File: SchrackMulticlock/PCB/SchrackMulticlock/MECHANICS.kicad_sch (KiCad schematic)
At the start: 22 parts, among them J2 MEM2067-02-180-00-A_REVB, SW2 SW_Push, SW3 SW_Push, SW4 SW_Push, SW5 SW_Push, SW6 SW_Push

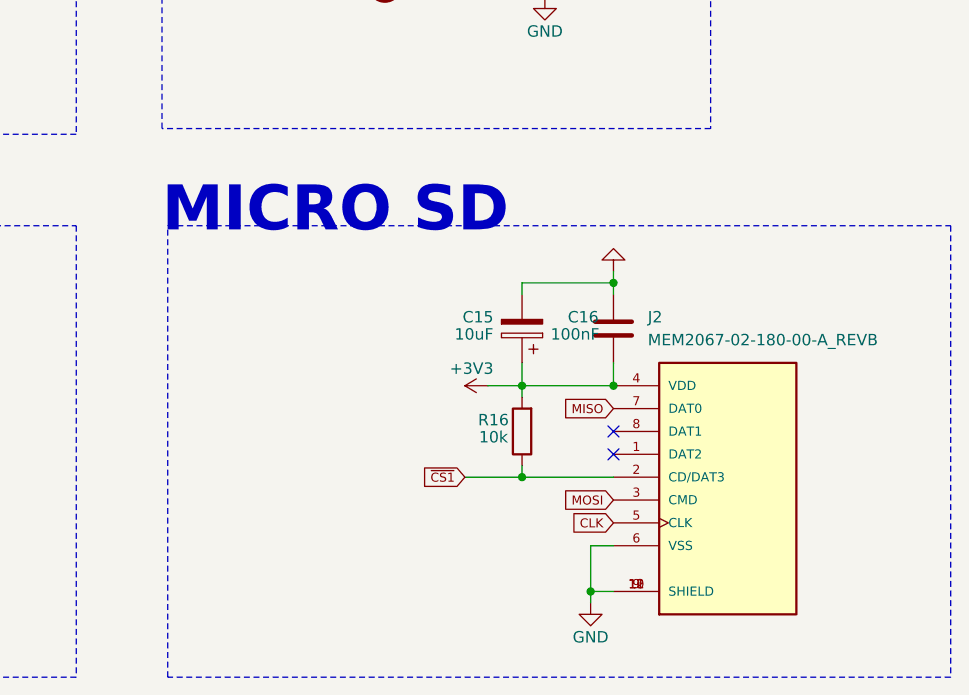
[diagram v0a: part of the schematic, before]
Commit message: SchrackMulticlock and Counter update
Schematic update for both
PCB update for Counter
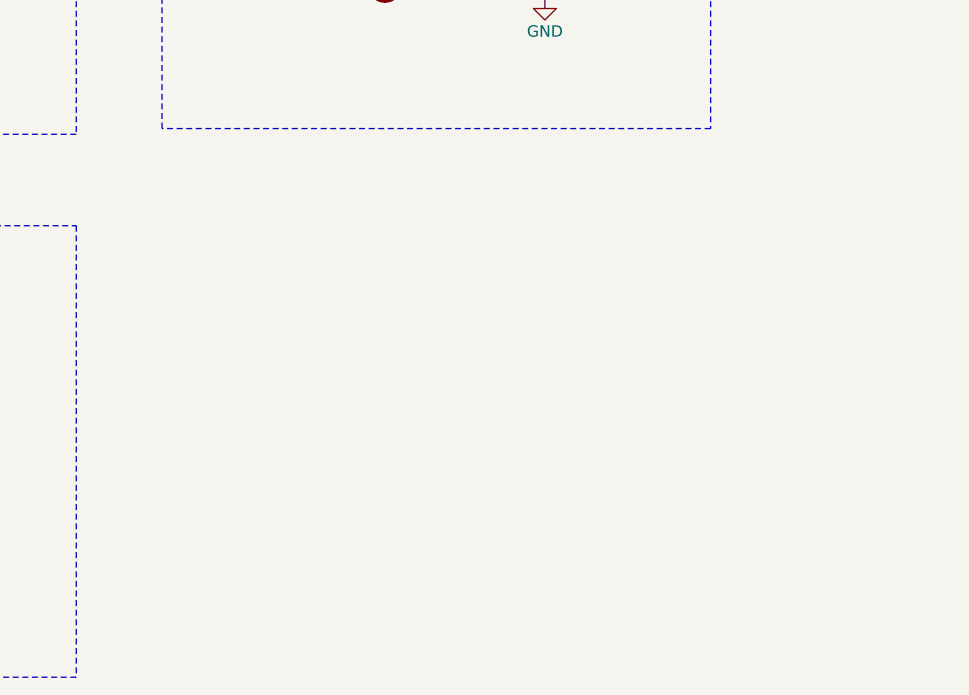
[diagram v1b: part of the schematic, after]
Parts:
- removed C15: 10uF, Capacitor_Tantalum_SMD:CP_EIA-3216-18_Kemet-A_Pad1.58x1.35mm_HandSolder, symbol Device:C_Polarized
- removed C16: 100nF, Capacitor_SMD:C_0805_2012Metric_Pad1.18x1.45mm_HandSolder, symbol Device:C
- removed J2: MEM2067-02-180-00-A_REVB, Schrack_brd:MICRO_SD_CARD, symbol SchrackThingy_library:MEM2067-02-180-00-A_REVB
- removed R16: 10k, Resistor_SMD:R_0805_2012Metric_Pad1.20x1.40mm_HandSolder, symbol Device:R
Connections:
- no-connect marks 2 -> 0
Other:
- note removed: "MICRO SD"

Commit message: schrack multiclock schematic update
Just regular updates
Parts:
- removed C10, C11, C13: 100nF, Capacitor_SMD:C_0805_2012Metric_Pad1.18x1.45mm_HandSolder, symbol Device:C
- removed R12, R13, R15: 2k, Resistor_SMD:R_0805_2012Metric_Pad1.20x1.40mm_HandSolder, symbol Device:R
- removed SW2, SW3, SW4: SW_Push, Connector_JST:JST_XH_B2B-XH-A_1x02_P2.50mm_Vertical, symbol Switch:SW_Push
- added C? (x3): 100nF, Capacitor_SMD:C_0805_2012Metric_Pad1.18x1.45mm_HandSolder, symbol Device:C
- added R? (x6): 10k, Resistor_SMD:R_0805_2012Metric_Pad1.20x1.40mm_HandSolder, symbol Device:R
- added SW? (x3): SW_Push, Connector_JST:JST_XH_B2B-XH-A_1x02_P2.50mm_Vertical, symbol Switch:SW_Push
- added U? (x7): 74HC14, Package_SO:SOIC-14_3.9x8.7mm_P1.27mm, symbol 74xx:74HC14
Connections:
- net +3V3: now also R?.2, R?.2, R?.2, U?.14 (VCC)
- net GND: now also C?.1, C?.1, C?.1, SW?.1, SW?.1, SW?.1, U?.7 (GND)
- net MODE: now also U?.6
- net RESET: now also U?.4
- new net: C?.2, R?.1, U?.3
- new net: C?.2, R?.1, U?.5
- new net: C?.2, R?.1, U?.1
- new net AUX: U?.2
- new net MD: R?.1, R?.2, SW?.2
- new net RST: R?.1, R?.2, SW?.2
- new net SCH_SW: R?.1, R?.2, SW?.2
- no-connect marks 0 -> 6
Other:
- note removed: "DEBOUNCE: 100nF and 2k?"

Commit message: SchrackMulticlock schematic
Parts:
- added C12, C15, C16: 100nF, Capacitor_SMD:C_0805_2012Metric_Pad1.18x1.45mm_HandSolder, symbol Device:C
- added R14, R17, R20, R21, R23, R24: 10k, Resistor_SMD:R_0805_2012Metric_Pad1.20x1.40mm_HandSolder, symbol Device:R
- added SW4, SW6, SW7: SW_Push, Connector_JST:JST_XH_B2B-XH-A_1x02_P2.50mm_Vertical, symbol Switch:SW_Push
- gave numbers to parts that had none: 13
- renumbered C12 to C13, C14 to C17, R14 to R18, SW5 to SW8, SW6 to SW9
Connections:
- net SCH_SW is gone; now on net MD: R19.1, R22.2, SW5.2
- net +3V3: now also R14.2, R20.2, R21.2
- net AUX: now also U8.10; no longer U8.2
- net GND: now also C12.1, C15.1, C16.1, SW4.1, SW6.1, SW7.1
- net MD: no longer R12.1, R15.2, SW2.2
- net MODE: now also U8.2; no longer U8.6
- net DIGIT_SELECT: now reaches U8.8
- net at U8.9: now also C12.2, R17.1
- net at U8.11: now also C15.2, R23.1
- net TIME_DOWN: now reaches U8.12
- net at U8.13: now also C16.2, R24.1
- net RESET renamed BTN2
- net RST renamed BT2
- net BT2: now also R14.1, R17.2, R20.1, R21.1, R23.2, R24.2, SW4.2, SW6.2, SW7.2
- new net BT1: R12.1, R15.2, SW2.2
- new net BTN1: U8.6
- no-connect marks 6 -> 0
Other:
- note added: "BTN1 press - digit++ BTN1 hold - digit select BTN2 press - start/stop (by context) BTN2 hold - reset MODE - ctu/ctd switch"
- note added: "harder for me to make it work in program..."
- note added: "the PCB is going to be much smaller, less reason to use the Schrack Box If the box is not going to be big, there is no reason to use SchrackButtons"
- note removed: "PREDIFINED TIME, CHANGING USING WEBSERVER"
- moved on the sheet: U8D, U8E, U8F, U8G

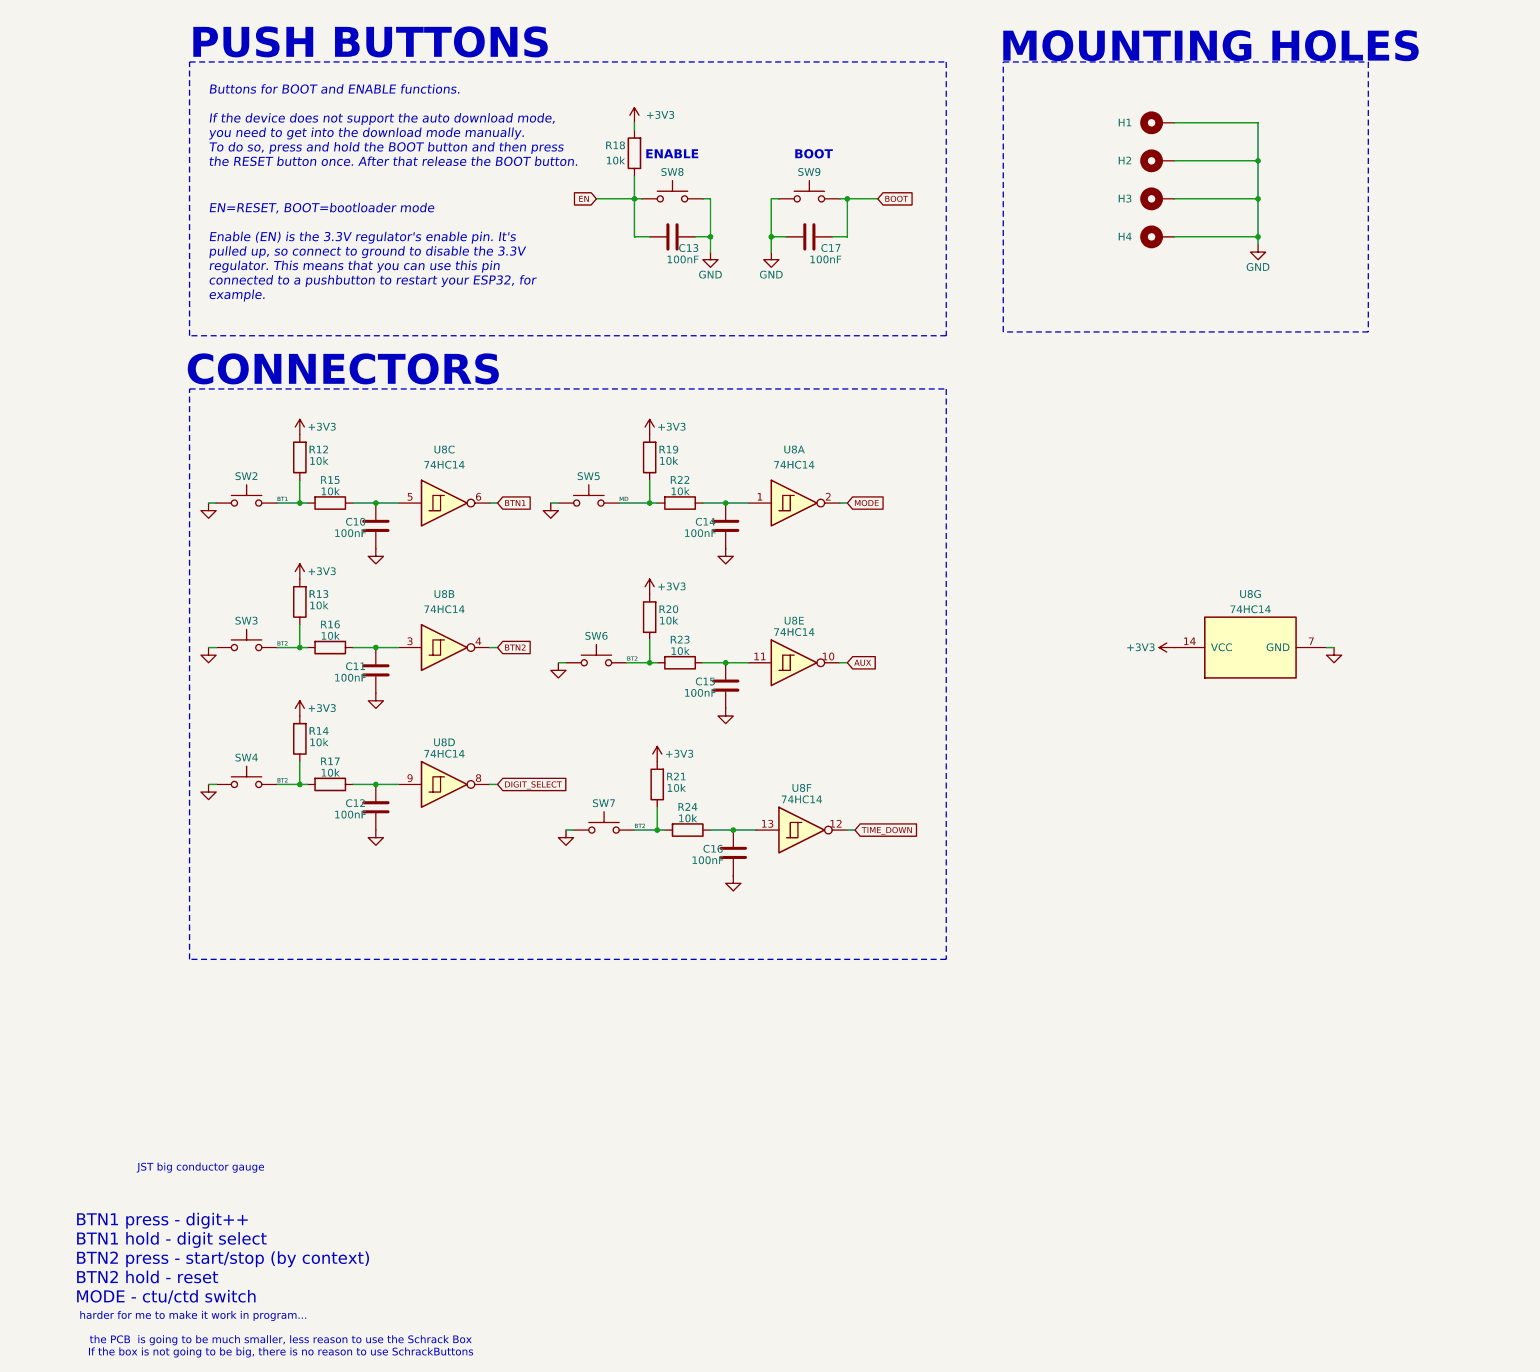
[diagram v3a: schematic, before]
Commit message: Schrackcounter Prototype update
Schematic + PCB update, final version
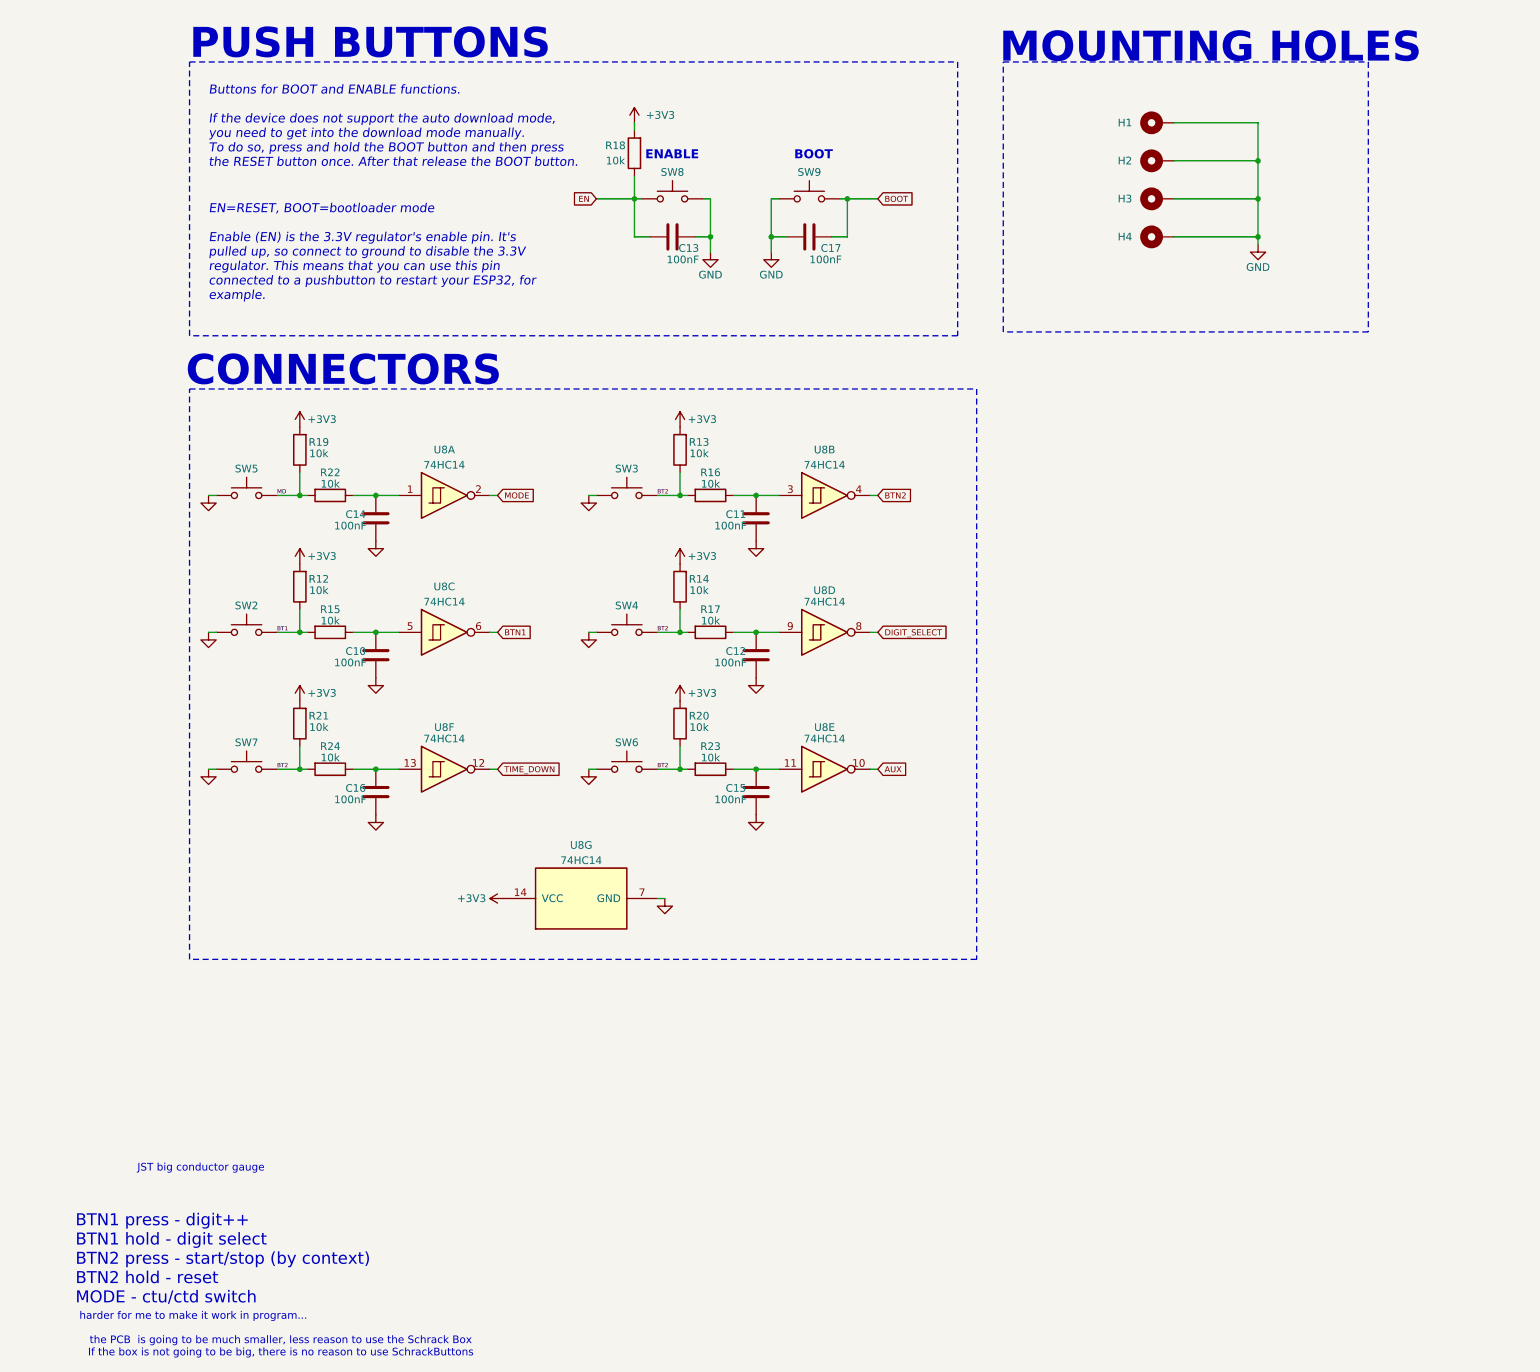
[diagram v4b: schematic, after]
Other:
- moved on the sheet: C10, C11, C12, C14, C15, C16, R12, R13, R14, R15, R16, R17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

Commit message: SchrackMulticlock update
Schematic and PCB update
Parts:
- renumbered C14 to C11, C10 to C12, C16 to C13, C13 to C14, C11 to C15, C12 to C16, C15 to C17, C17 to C18, R19 to R13, R12 to R14, R21 to R15, R22 to R16, R15 to R17, R24 to R18, R18 to R19, R13 to R20, R14 to R21, R20 to R22, R16 to R23, R17 to R24, R23 to R25, SW5 to SW2, SW2 to SW3, SW7 to SW4, SW3 to SW5, SW4 to SW6, SW6 to SW7
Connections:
- net BT2: no longer R15.1, R18.2, SW4.2
- net BT1 renamed TP
- net BTN1 renamed TIME_UP
- new net TD: R15.1, R18.2, SW4.2

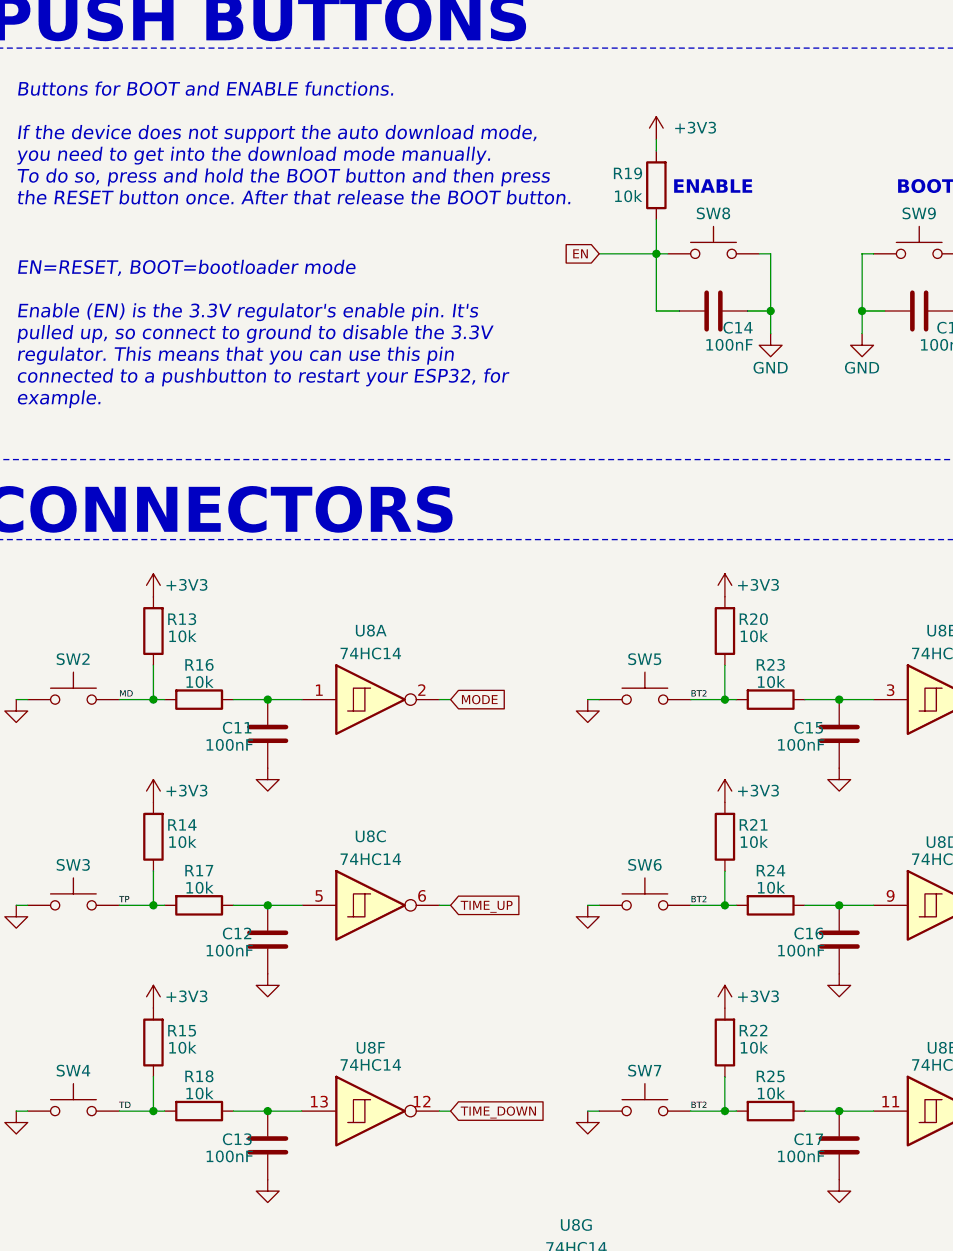
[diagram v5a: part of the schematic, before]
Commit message: SchrackMulticlock and Counter pcb updates
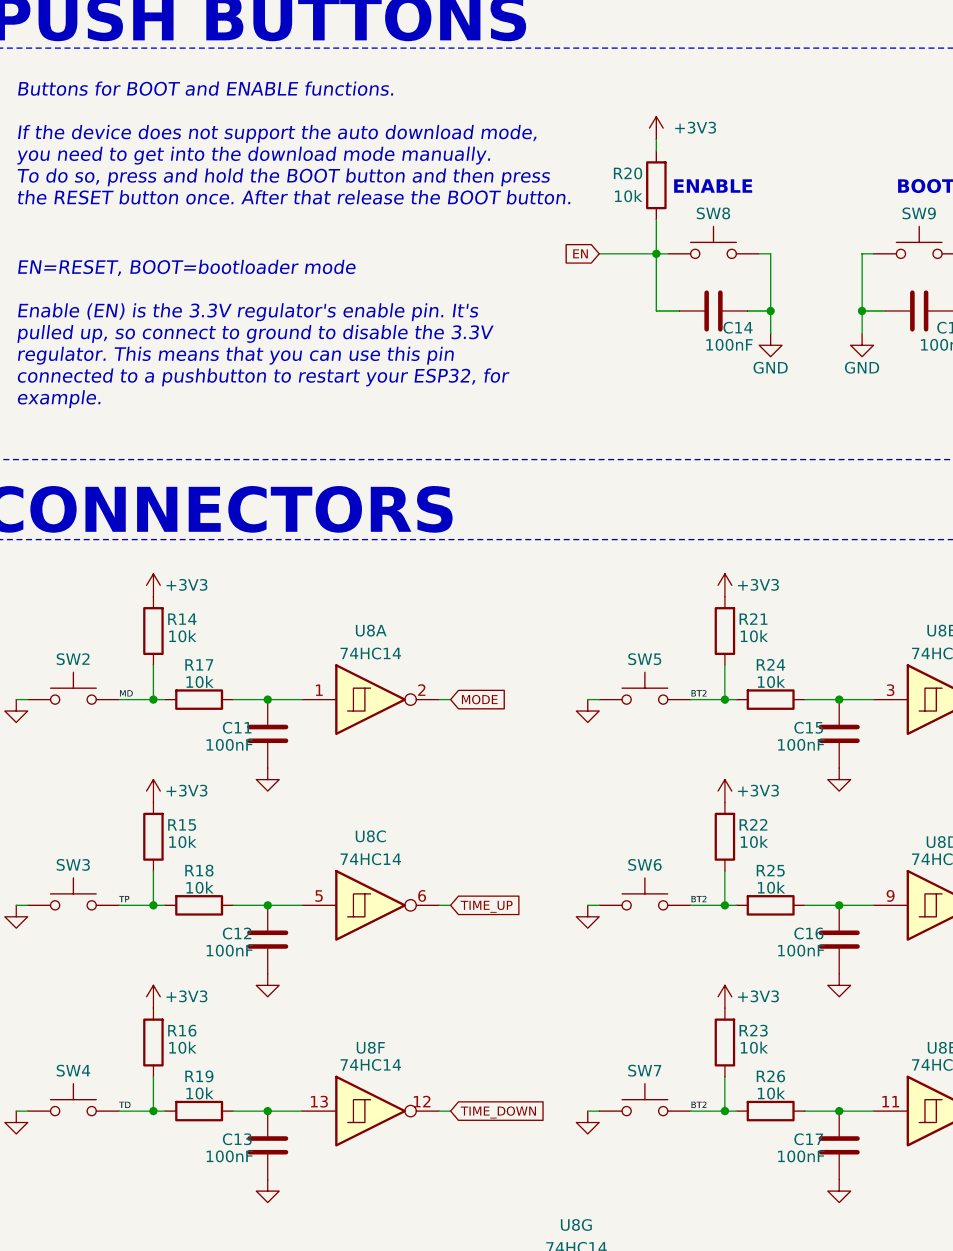
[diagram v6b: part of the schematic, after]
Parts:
- renumbered R13 to R14, R14 to R15, R15 to R16, R16 to R17, R17 to R18, R18 to R19, R19 to R20, R20 to R21, R21 to R22, R22 to R23, R23 to R24, R24 to R25, R25 to R26

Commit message: Multiclock PCB update
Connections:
- net AUX: now also R23.1, R26.2, SW7.2
- net BT2: no longer R22.1, R23.1, R25.2, R26.2, SW6.2, SW7.2
- new net DGT: R22.1, R25.2, SW6.2
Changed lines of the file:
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@@
 		)
 	)
-	(label "BT2"
+	(label "DGT"
 		(at 118.11 120.65 0)
 		(fields_autoplaced yes)
@@
 		)
 	)
-	(label "BT2"
+	(label "AUX"
 		(at 118.11 143.51 0)
 		(fields_autoplaced yes)
